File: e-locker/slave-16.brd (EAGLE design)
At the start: 93.3 x 100 mm, 86 parts, among them IC1 PCF8574P, IC2 PCF8574P, IC3 PCF8574P, IC4 PCF8574P, X1 JST-XH-02-PIN-LONG-PAD, X10 JST-XH-04-PIN-LONG-PAD, X11 JST-XH-02-PIN-LONG-PAD, X12 JST-XH-04-PIN-LONG-PAD, X13 JST-XH-04-PIN-LONG-PAD, X14 JST-XH-04-PIN-LONG-PAD, X15 JST-XH-04-PIN-LONG-PAD, X16 JST-XH-04-PIN-LONG-PAD, X17 JST-XH-04-PIN-LONG-PAD, X18 JST-XH-04-PIN-LONG-PAD, X19 JST-XH-04-PIN-LONG-PAD, X2 JST-XH-05-PIN-LONG-PAD, X20 JST-XH-05-PIN-LONG-PAD, X21 JST-XH-02-PIN-LONG-PAD, X22 JST-XH-02-PIN-LONG-PAD, X3 JST-XH-04-PIN-LONG-PAD, X4 JST-XH-04-PIN-LONG-PAD, X5 JST-XH-04-PIN-LONG-PAD, X6 JST-XH-04-PIN-LONG-PAD, X7 JST-XH-04-PIN-LONG-PAD, X8 JST-XH-04-PIN-LONG-PAD, X9 JST-XH-04-PIN-LONG-PAD

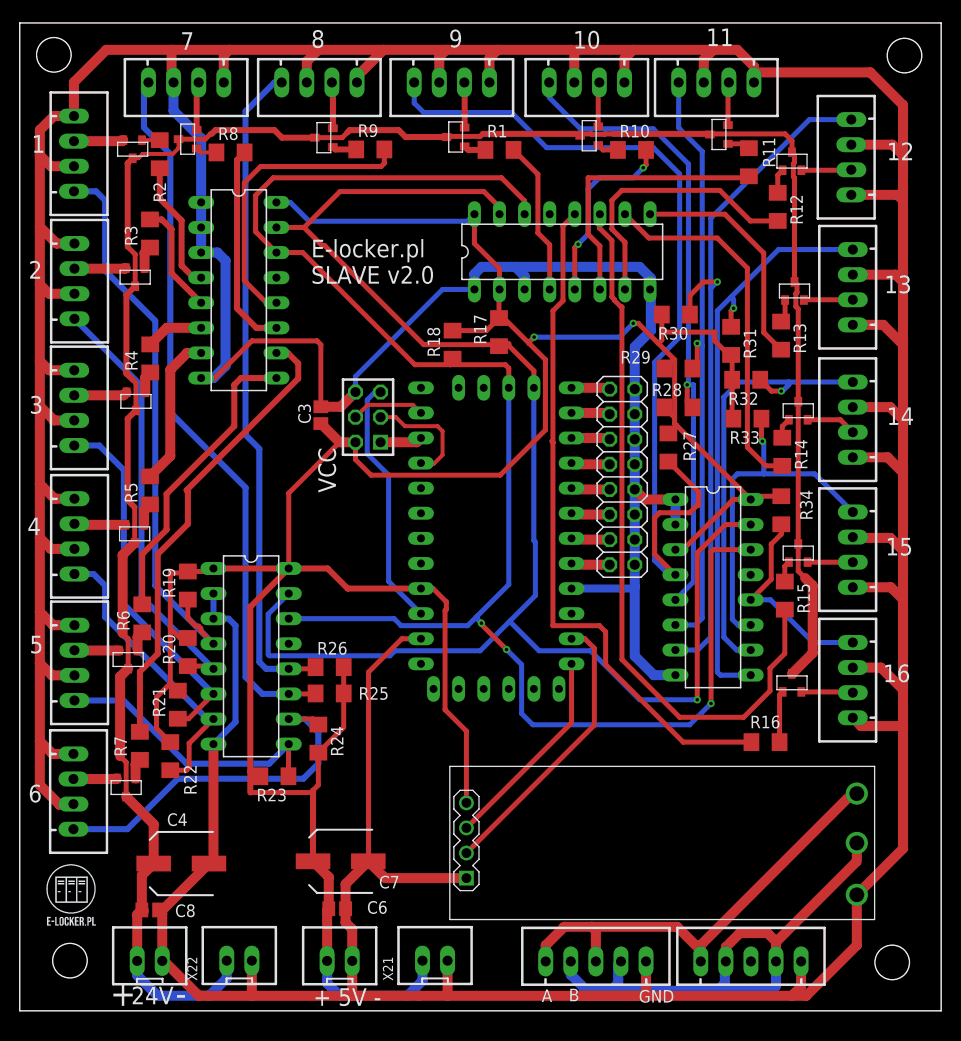
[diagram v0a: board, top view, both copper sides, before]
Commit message: arduino footprint change
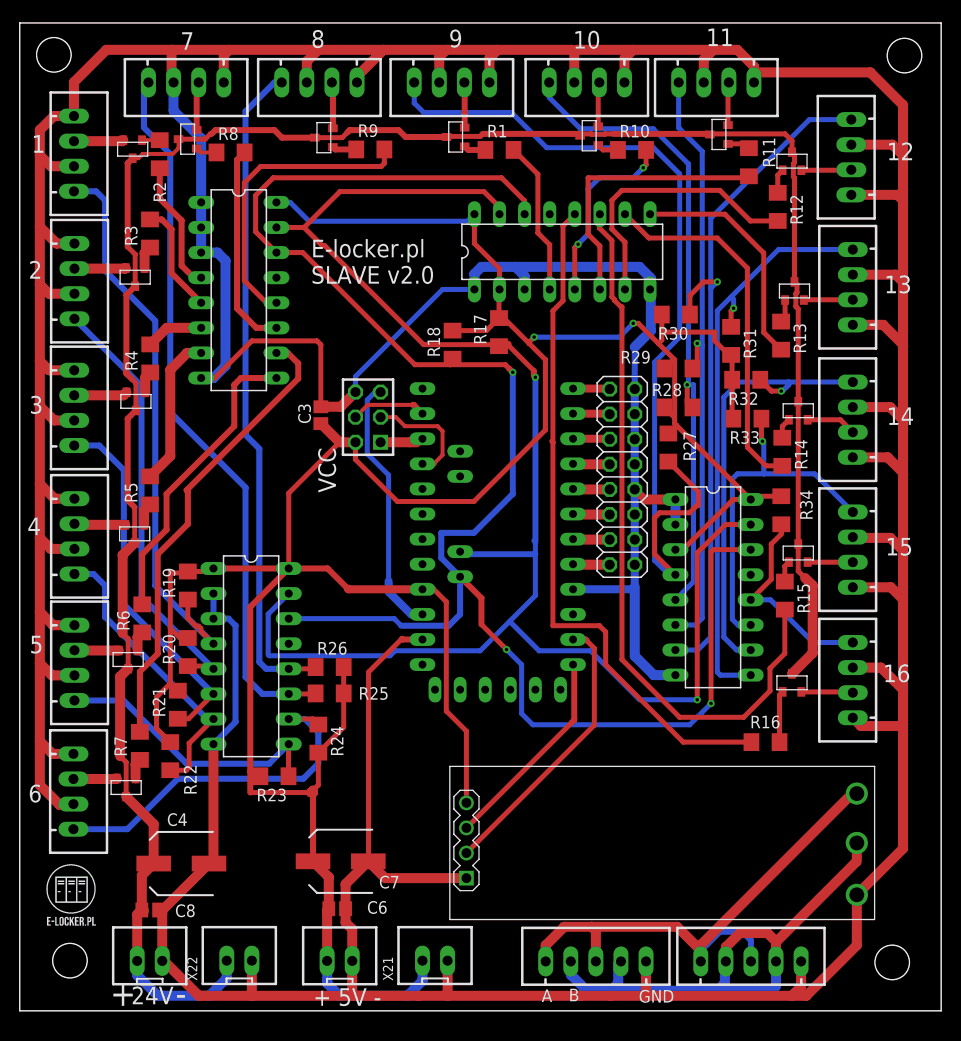
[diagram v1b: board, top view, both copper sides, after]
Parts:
- removed U$11: PRO-MINI, Arduino-clone:PRO-MINI
- added U$20: PRO-MINI-2, Arduino-clone:PRO-MINI-2
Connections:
- removed net A6: U$11.A6
- removed net RAW: U$11.RAW
- net A0: now also U$20.A0; no longer U$11.A0
- net A1: now also U$20.A1; no longer U$11.A1
- net A2: now also U$20.A2; no longer U$11.A2
- net A3: now also U$20.A3; no longer U$11.A3
- net A4: now also U$20.A4; no longer U$11.A4
- net A5: now also U$20.A5; no longer U$11.A5
- net A7: now also U$20.A7; no longer U$11.A7
- net D0: now also U$20.RX1; no longer U$11.RX1
- net D1: now also U$20.TX0; no longer U$11.TX0
- net D11: now also U$20.D11; no longer U$11.D11
- net D12: now also U$20.D12; no longer U$11.D12
- net D13: now also U$20.D13; no longer U$11.D13
- net GND: now also U$20.GND, U$20.GND1; no longer U$11.GND, U$11.GND1
- net N$10: now also U$20.D2; no longer U$11.D2
- net N$17: now also U$20.D3; no longer U$11.D3
- net N$20: now also U$20.D4; no longer U$11.D4
- net N$21: now also U$20.D5; no longer U$11.D5
- net N$22: now also U$20.D6; no longer U$11.D6
- net N$23: now also U$20.D7; no longer U$11.D7
- net N$24: now also U$20.D8; no longer U$11.D8
- net N$25: now also U$20.D9; no longer U$11.D9
- net RST: now also U$20.RST; no longer U$11.RST
- net VCC: now also U$20.VCC; no longer U$11.VCC
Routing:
- net A: track 48.5 -> 57.9 mm
- net A4: track 158.9 -> 166.8 mm, vias 1 -> 2
- net A5: track 163.9 -> 171.5 mm
- net GND: track 757.9 -> 751.3 mm
- net VCC: track 315.0 -> 317.4 mm
- net RST: track 25.6 -> 26.4 mm
- net D12: track 4.27 -> 5.07 mm

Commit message: slave p-channel mosfet
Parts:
- added Q1, Q2, Q3, Q4, Q5, Q6, Q7, Q8: BC547B, transistor-npn:TO92
- added R35, R36, R37, R38, R39, R40, R41, R42, R43, R44, R45, R46, R47, R48, R49, R50: (no value), eagle-ltspice:R1206
- added T1, T2, T3, T4, T5, T6, T7, T8: BC547, transistor:TO92
- U$1, U$12, U$13, U$14, U$15, U$16, U$17, U$18, U$19, U$2, U$3, U$4, U$5, U$6, U$7, U$8: value IRLML6344 -> IRLML6402
- moved R7 40.5 mm to (28.5, 63.9)
- moved R6 24.8 mm to (26.2, 60.3)
- moved R14 21.3 mm to (67.8, 75.7), turned to 180 degrees
- moved R16 16.5 mm to (59.7, 32.2), turned to 90 degrees
- moved R15 16.5 mm to (61.0, 40.4), turned to 90 degrees
- moved R13 13.8 mm to (67.8, 78.6), turned to 180 degrees
- moved R5 10.2 mm to (20.7, 59.7)
- moved C8 9.15 mm to (22.4, 9.96)
- moved R12 8.97 mm to (67.8, 82.1), turned to 180 degrees
- moved C4 6.48 mm to (22.8, 15.2)
- moved U$15 5.89 mm to (79.2, 80.2), turned to 270 degrees
- moved R9 5.86 mm to (32.8, 82.0), turned to 180 degrees
- moved R1 4.90 mm to (53.4, 86.7), turned to 90 degrees
- moved U$8 4.70 mm to (35.5, 88.3)
- moved U$2 4.57 mm to (10.5, 69.8), turned to 90 degrees
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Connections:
- new net A6: U$20.A6
- new net N$26: R1.2, T1.2
- new net N$27: R35.1, T1.3, U$12.P1
- new net N$28: R42.1, T8.3, U$19.P1
- new net N$29: R40.1, T6.3, U$17.P1
- new net N$3: R15.1, T7.2
- new net N$54: U$8.P3, X10.2
- new net N$55: R38.1, T4.3, U$15.P1
- new net N$56: Q8.3, R50.1, U$8.P1
- new net N$57: R12.1, T4.2
- new net N$58: R37.1, T3.3, U$14.P1
- new net N$59: Q7.3, R49.1, U$7.P1
- new net N$60: R11.1, T3.2
- new net N$61: R10.1, T2.2
- new net N$62: R36.1, T2.3, U$13.P1
- new net N$63: Q6.3, R48.1, U$6.P1
- new net N$64: Q5.3, R47.1, U$5.P1
- net GND: now also Q1.1, Q2.1, Q3.1, Q4.1, Q5.1, Q6.1, Q7.1, Q8.1, T1.1, T2.1, T3.1, T4.1, T5.1, T6.1, T7.1, T8.1
- net N$1: now also Q8.2, R9.1; no longer R2.1, U$1.P1
- net N$11: now also Q1.3, R43.1, U$1.P1; no longer U$1.P2, X3.2
- net N$12: now also Q2.3, R44.1, U$2.P1; no longer U$2.P2, X4.2
- net N$13: now also Q3.3, R45.1, U$3.P1; no longer U$3.P2, X5.2
- net N$14: now also Q4.3, R46.1, U$4.P1; no longer U$4.P2, X6.2
- net N$15: now also U$1.P3, X3.2; no longer U$5.P2, X7.2
- net N$16: now also U$2.P3, X4.2; no longer U$6.P2, X8.2
- net N$18: now also U$3.P3, X5.2; no longer U$7.P2, X9.2
- net N$19: now also U$4.P3, X6.2; no longer U$8.P2, X10.2
- net N$2: now also Q7.2, R8.1; no longer R3.1, U$2.P1
- net N$38: now also R16.1, T8.2; no longer R1.1, U$12.P1
- net N$39: now also R14.1, T6.2; no longer R10.1, U$13.P1
- net N$4: now also Q6.2, R7.1; no longer R4.1, U$3.P1
- net N$40: now also U$5.P3, X7.2; no longer R11.1, U$14.P1
- net N$41: now also U$6.P3, X8.2; no longer R12.1, U$15.P1
- net N$42: now also U$7.P3, X9.2; no longer R13.1, U$16.P1
- net N$43: now also R39.1, T5.3, U$16.P1; no longer R14.1, U$17.P1
- net N$44: now also R41.1, T7.3; no longer R15.1
- net N$45: now also R13.1, T5.2; no longer R16.1, U$19.P1
- net N$46: now also U$12.P3; no longer U$12.P2
- net N$47: now also U$13.P3; no longer U$13.P2
- net N$48: now also U$14.P3; no longer U$14.P2
- net N$49: now also U$15.P3; no longer U$15.P2
- net N$5: now also Q5.2, R6.1; no longer R5.1, U$4.P1
- net N$50: now also U$16.P3; no longer U$16.P2
- net N$51: now also U$17.P3; no longer U$17.P2
- net N$52: now also U$18.P3; no longer U$18.P2
- net N$53: now also U$19.P3; no longer U$19.P2
- net N$6: now also Q4.2, R5.1; no longer R6.1, U$5.P1
- net N$7: now also Q3.2, R4.1; no longer R7.1, U$6.P1
- net N$8: now also Q2.2, R3.1; no longer R8.1, U$7.P1
- net N$9: now also Q1.2, R2.1; no longer R9.1, U$8.P1
- net S8: now also R1.1; no longer R1.2
- net V24: now also R35.2, R36.2, R37.2, R38.2, R39.2, R40.2, R41.2, R42.2, R43.2, R44.2, R45.2, R46.2, R47.2, R48.2, R49.2, R50.2, U$1.P2, U$12.P2, U$13.P2, U$14.P2, U$15.P2, U$16.P2, U$17.P2, U$18.P2, U$19.P2, U$2.P2, U$3.P2, U$4.P2, U$5.P2, U$6.P2, U$7.P2, U$8.P2; no longer U$1.P3, U$12.P3, U$13.P3, U$14.P3, U$15.P3, U$16.P3, U$17.P3, U$18.P3, U$19.P3, U$2.P3, U$3.P3, U$4.P3, U$5.P3, U$6.P3, U$7.P3, U$8.P3
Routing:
- net GND: track 751.3 -> 916.1 mm
- net V24: track 226.4 -> 279.3 mm
- net N$35: track 46.7 -> 3.21 mm
- net N$63: track 0.00 -> 41.9 mm
- net S14: track 73.5 -> 39.9 mm
- net S13: track 37.1 -> 7.12 mm
- net N$44: track 2.13 -> 31.3 mm
- net N$34: track 30.6 -> 2.44 mm
- net N$64: track 0.00 -> 27.0 mm
- net S12: track 23.6 -> 4.38 mm
- net N$28: track 0.00 -> 17.4 mm
- net S15: track 69.7 -> 53.4 mm
- net N$3: track 0.00 -> 15.8 mm
- net N$29: track 0.00 -> 14.6 mm
- net N$62: track 0.00 -> 13.0 mm
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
